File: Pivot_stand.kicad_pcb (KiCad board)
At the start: 2 copper layers, 64.3 x 49.2 mm, 18 parts, among them J1 USB_B_Micro, J2 Power_out, U1 TLV1117-33

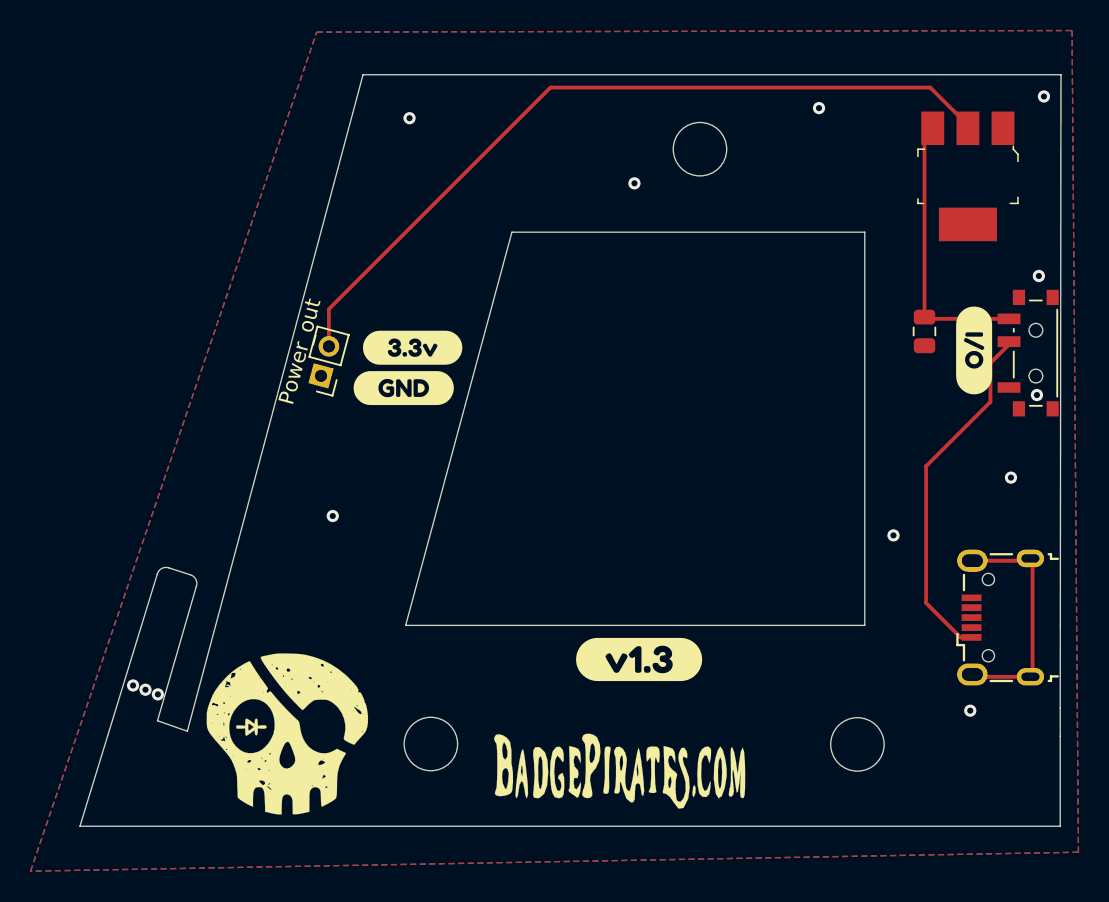
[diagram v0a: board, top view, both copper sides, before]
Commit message: Layout updates
Added new parts to PCB to match schematic changes.
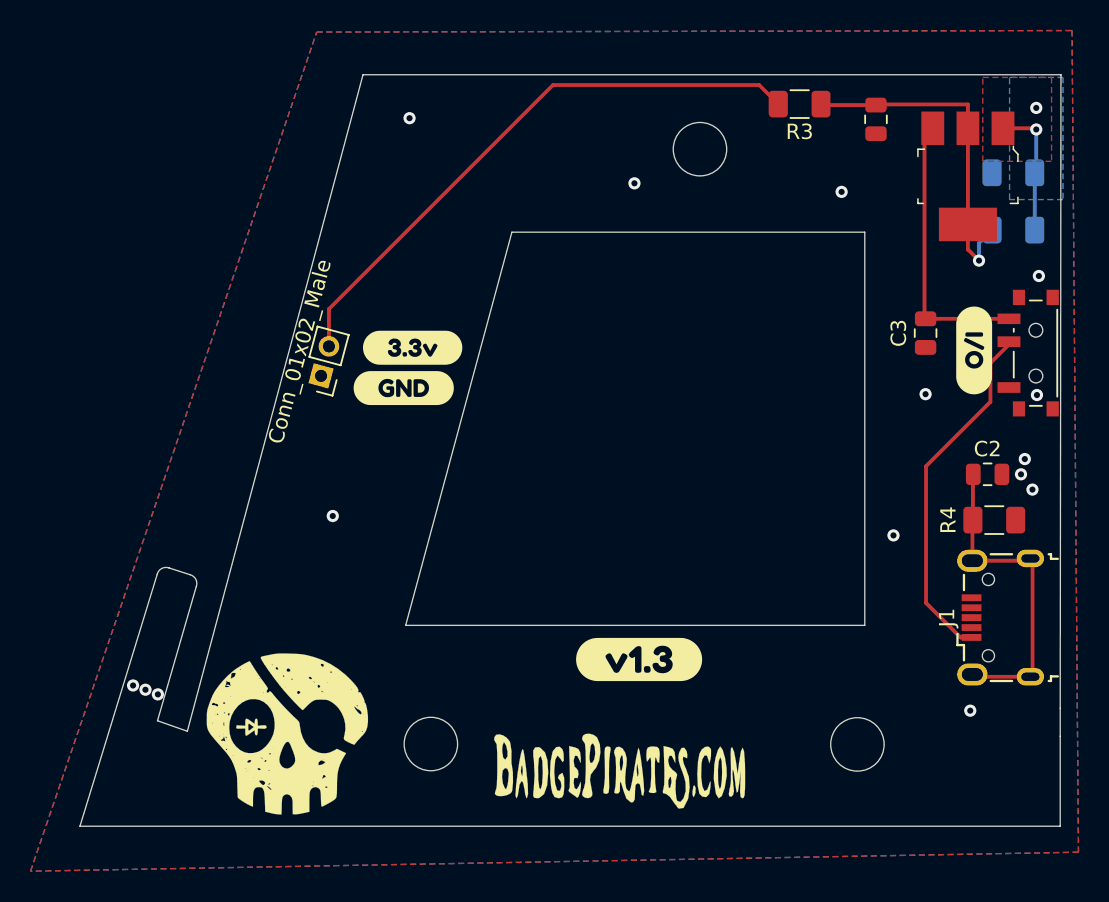
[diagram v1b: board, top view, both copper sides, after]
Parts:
- added C2: 0.1uF, BadgePirates:C_0805_2012Metric, F.Cu at (171.1, 126.2)
- added C3: 0.1uF, BadgePirates:C_0805_2012Metric, F.Cu at (167.0, 117.0)
- added R1: R, BadgePirates:R_1206_3216Metric, B.Cu at (172.8, 110.2)
- added R2: 0, BadgePirates:R_1206_3216Metric, B.Cu at (172.8, 106.5)
- added R3: 0, BadgePirates:R_1206_3216Metric, F.Cu at (158.8, 102.0)
- added R4: 1M, BadgePirates:R_1206_3216Metric, F.Cu at (171.5, 129.2)
- C1: value C -> 10uF
- J1: footprint BadgePirates:USB_Micro-B_Wuerth_629105150521_fgFixed -> Connector_USB:USB_Micro-B_Wuerth_629105150521
- J2: value Power_out -> Conn_01x02_Male
- U1: value TLV1117-33 -> IFX27001TFV33
- moved C1 14.2 mm to (163.8, 103.0)
- moved G*** 5.17 mm to (166.5, 107.8)
- renumbered I/O to I/O1
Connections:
- I/O1 pad 3: Net-(C1-Pad1) -> Net-(C3-Pad1)
- J1 pad 6: unconnected-(J1-Pad6) -> Net-(C2-Pad1)
- U1 pad 1: GND -> /ADJ
- U1 pad 2: +3V3 -> Net-(C1-Pad1)
- U1 pad 3: Net-(C1-Pad1) -> Net-(C3-Pad1)
- U1 pad 4: (no net) -> Net-(C1-Pad1)
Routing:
- net Net-(C2-Pad1): track 0.00 -> 21.2 mm
- net Net-(C3-Pad1): track 0.00 -> 19.2 mm
- net unconnected-(J1-Pad6): track 15.5 -> 0.00 mm
- net +3V3: track 51.5 -> 38.5 mm
- net /ADJ: track 0.00 -> 8.84 mm, vias 0 -> 2
- net Net-(C1-Pad1): track 18.4 -> 22.5 mm, vias 0 -> 1
- net GND: vias 13 -> 15
- added copper zone on B.Cu, net /ADJ
- added copper zone on F.Cu, net /ADJ
